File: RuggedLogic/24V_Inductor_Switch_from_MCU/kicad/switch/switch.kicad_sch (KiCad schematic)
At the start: 17 parts, among them J1 Conn_01x03_Pin, J2 Conn_01x02_Pin, J3 Conn_01x03_Pin, T1 IRLML0040, T2 2SCR587D3

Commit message: Redone Z-input PCB; production update
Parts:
- D2, D3, D4: footprint Diode_SMD:D_SOD-123F -> Secoh:D_SOD-123F_hand_soldering
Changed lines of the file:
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@@
 			)
 		)
-		(property "Footprint" "Diode_SMD:D_SOD-123F"
+		(property "Footprint" "Secoh:D_SOD-123F_hand_soldering"
 			(at 170.815 76.2 0)
 			(effects
@@
 			)
 		)
-		(property "Footprint" "Diode_SMD:D_SOD-123F"
+		(property "Footprint" "Secoh:D_SOD-123F_hand_soldering"
 			(at 176.53 125.73 0)
 			(effects
@@
 			)
 		)
-		(property "Footprint" "Diode_SMD:D_SOD-123F"
+		(property "Footprint" "Secoh:D_SOD-123F_hand_soldering"
 			(at 161.925 96.52 0)
 			(effects

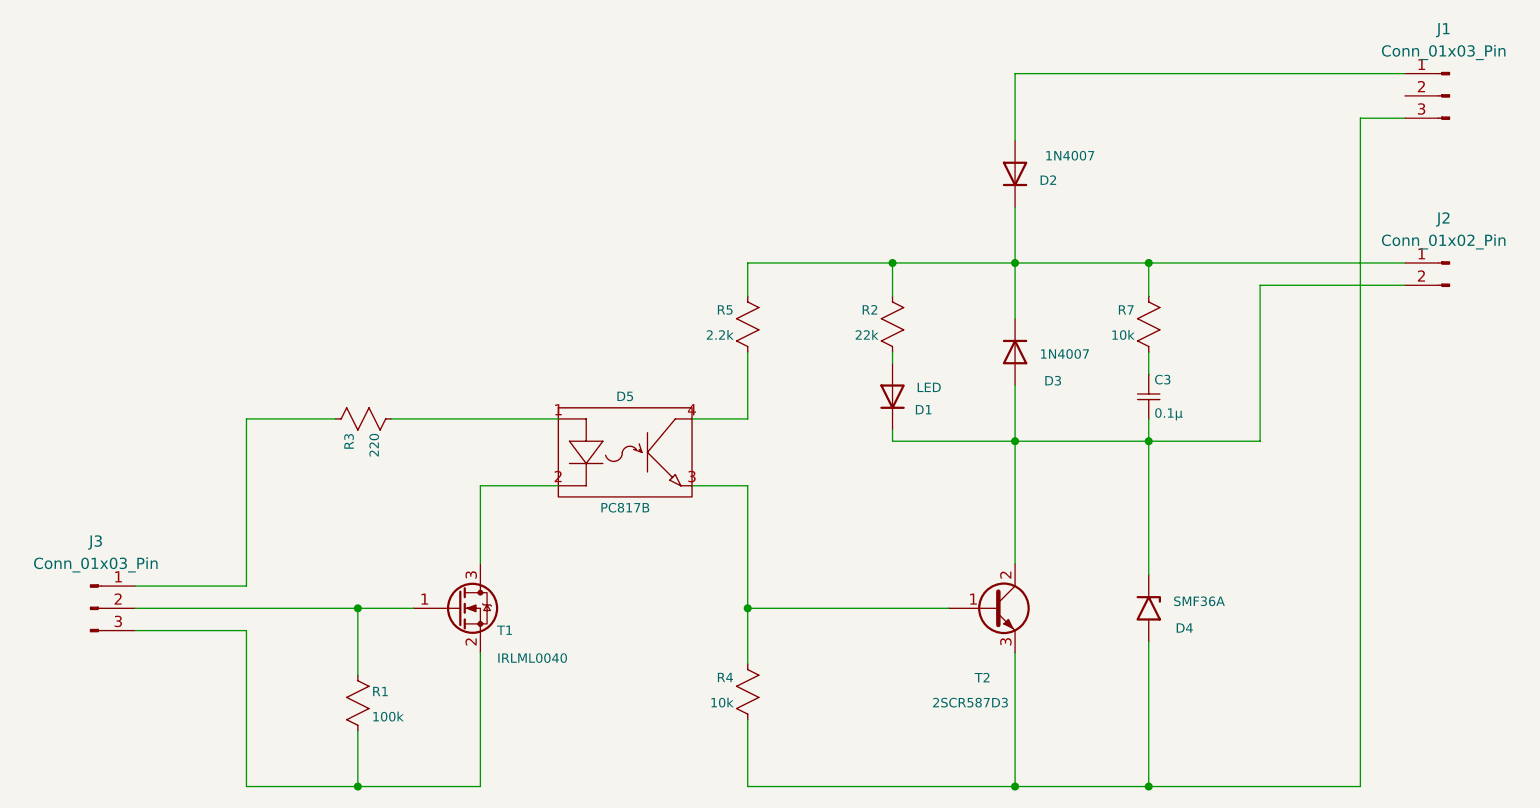
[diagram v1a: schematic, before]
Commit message: Fixed errors in Rugged Z sensor Fixes to Rugged Switch
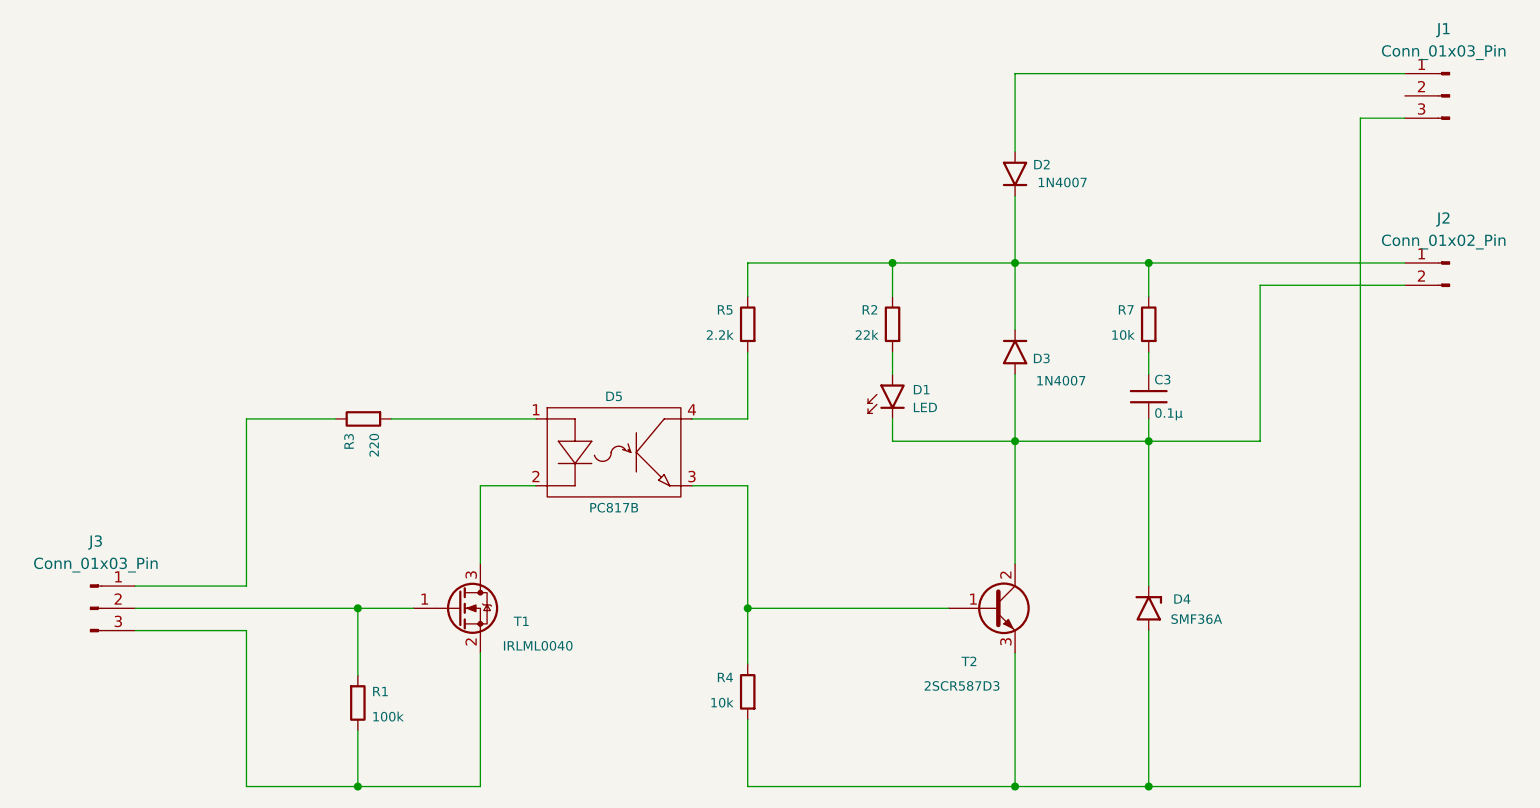
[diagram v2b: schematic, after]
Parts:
- C3: symbol ltspice:cap -> Secoh:0805/C
- D1: footprint LED_SMD:LED_0805_2012Metric_Pad1.15x1.40mm_HandSolder -> Secoh:LED_0805; symbol Device:D -> Secoh:0805/LED
- D2, D3: symbol Diode:1N4007 -> Secoh:SOD-123/Diode
- D4: symbol Diode:SMF36A -> Secoh:SOD-123/Zener
- D5: symbol ltspice:Optos/PC817B -> Secoh:Optos/PC817B
- R1, R2, R3, R4, R5, R7: symbol ltspice:res -> Secoh:0805/R
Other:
- moved on the sheet: D5

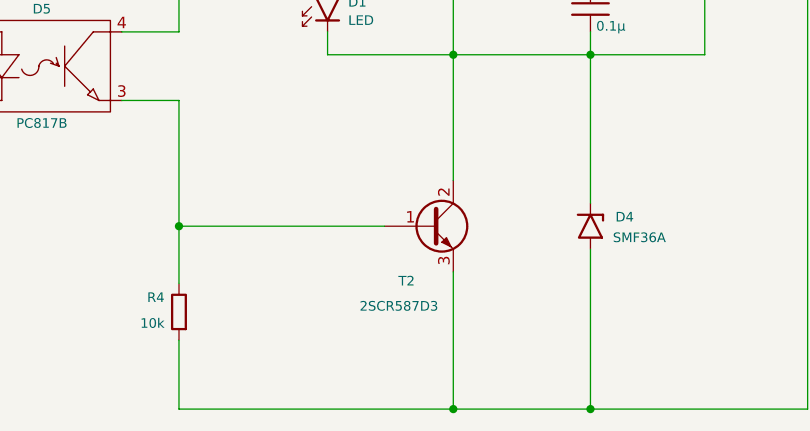
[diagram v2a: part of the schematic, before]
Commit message: Updated Rugged Z sensor and Switch; schematics and PCB
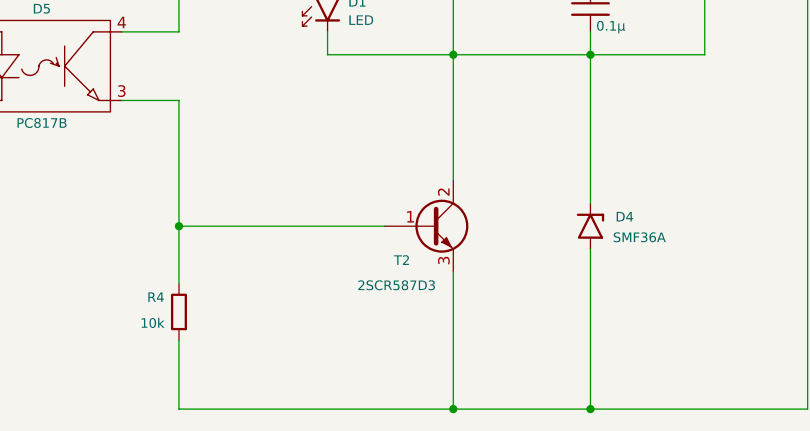
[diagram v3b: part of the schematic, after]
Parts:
- T1: symbol Device:Q_NMOS_GSD -> Secoh:N-chan/IRLML0040_SOT-23
- T2: symbol Device:Q_NPN_BCE -> Secoh:NPN/2SCR587D3
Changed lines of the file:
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@@
 	)
 	(symbol
-		(lib_id "Device:Q_NMOS_GSD")
+		(lib_id "Secoh:N-chan/IRLML0040_SOT-23")
 		(at 102.87 125.73 0)
 		(unit 1)
@@
 		)
 		(property "Footprint" "Package_TO_SOT_SMD:SOT-23_Handsoldering"
-			(at 107.95 123.19 0)
+			(at 102.87 125.73 0)
 			(effects
 				(font
@@
 	)
 	(symbol
-		(lib_id "Device:Q_NPN_BCE")
+		(lib_id "Secoh:NPN/2SCR587D3")
 		(at 163.83 125.73 0)
 		(unit 1)
@@
 		(dnp no)
 		(property "Reference" "T2"
-			(at 160.274 131.826 0)
+			(at 159.766 129.54 0)
 			(effects
 				(font
@@
 		)
 		(property "Value" "2SCR587D3"
-			(at 155.956 134.62 0)
+			(at 155.702 132.334 0)
 			(effects
 				(font
@@
 		)
 		(property "Footprint" "Package_TO_SOT_SMD:TO-252-2"
-			(at 168.91 123.19 0)
-			(effects
-				(font
+			(at 163.83 125.73 0)
+			(effects
+				(font
